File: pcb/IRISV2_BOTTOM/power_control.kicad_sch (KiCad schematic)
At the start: 49 parts, among them J10 Screw_Terminal_01x02, J11 Screw_Terminal_01x02, J12 Screw_Terminal_01x02, J13 Screw_Terminal_01x02, J14 Screw_Terminal_01x02, J15 Screw_Terminal_01x02, J16 Screw_Terminal_01x02, J9 Screw_Terminal_01x02, Q1 BC846, Q10 PJA3404A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

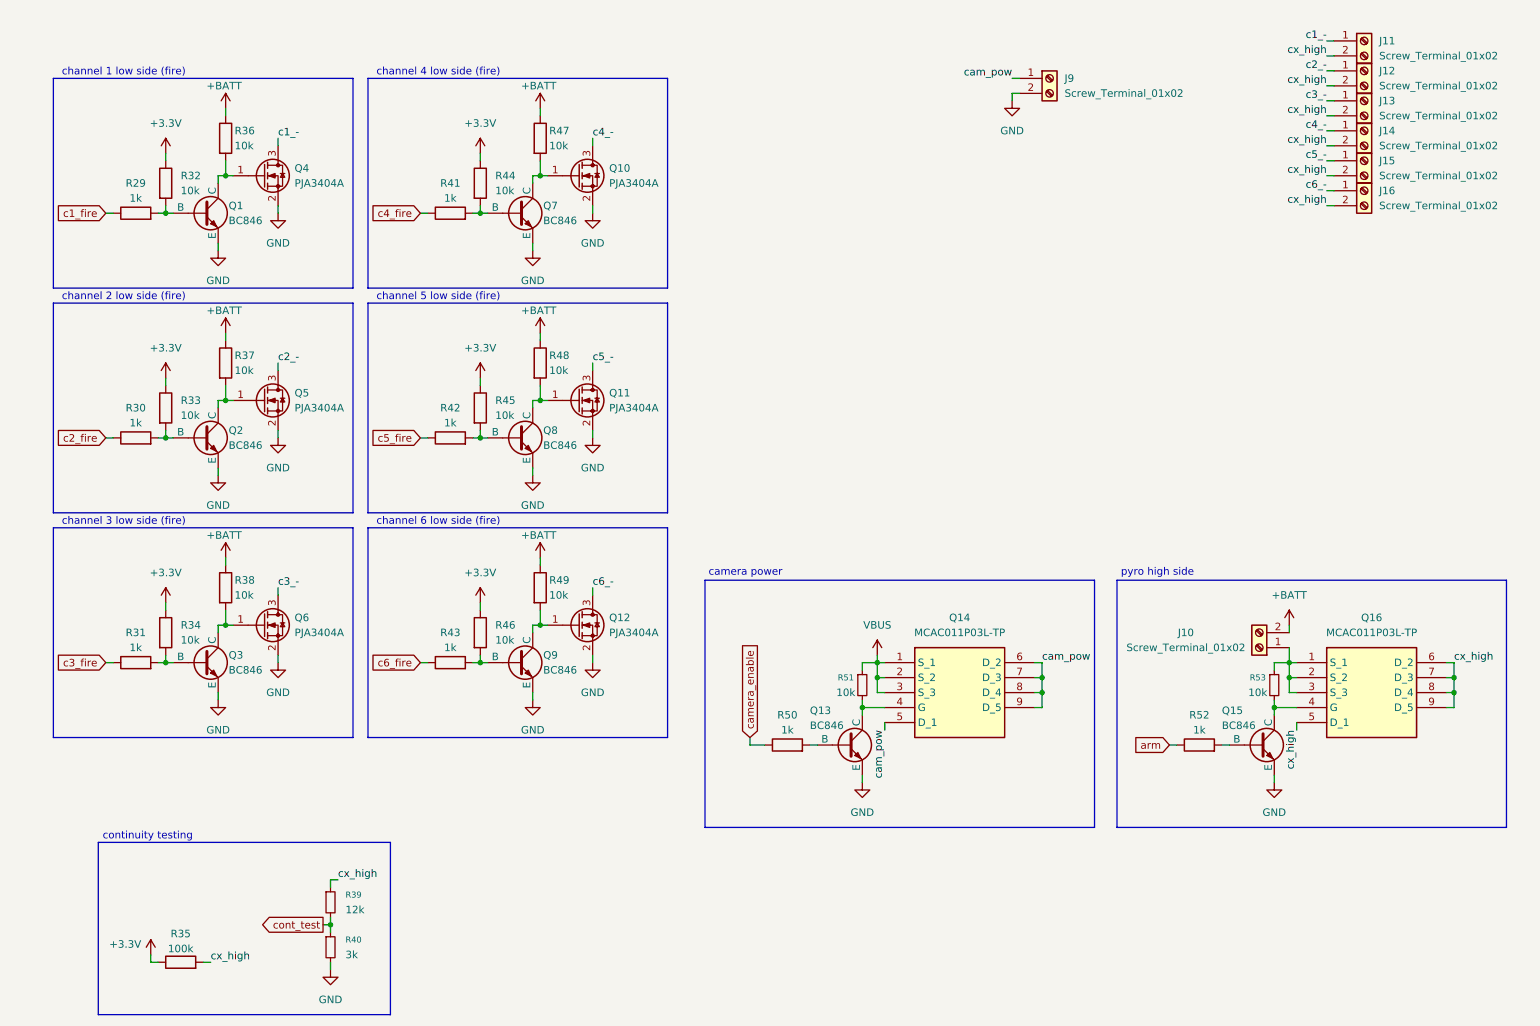
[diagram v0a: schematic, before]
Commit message: split into subprojects, fixed up stuff, started real pcb work
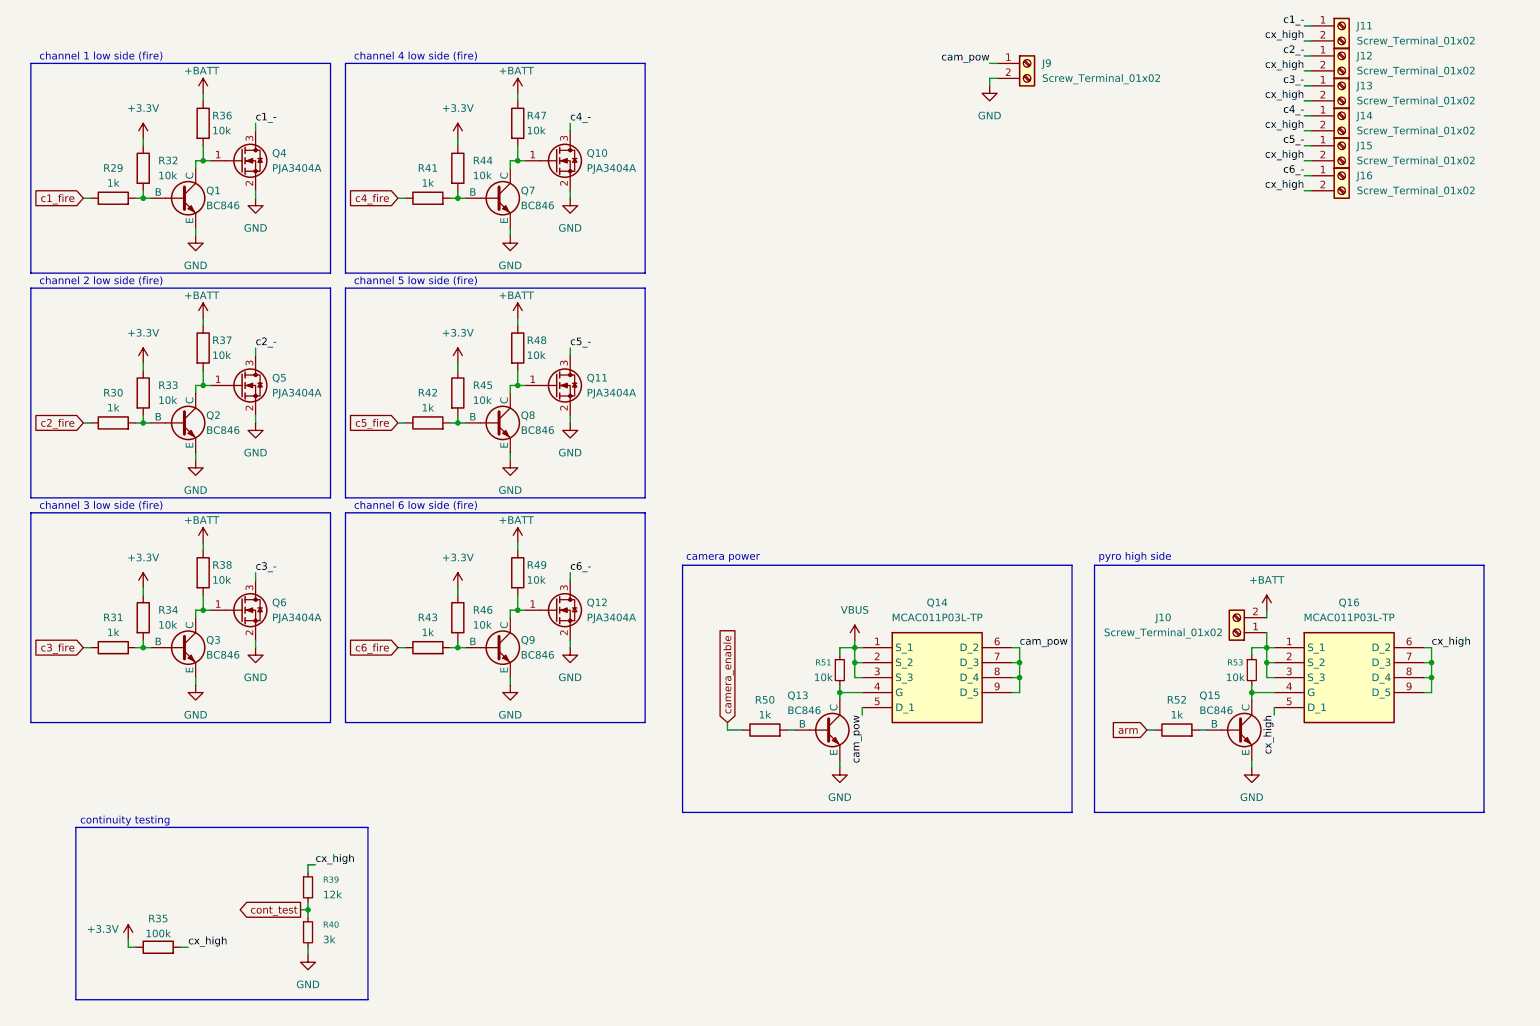
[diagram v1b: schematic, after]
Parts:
- Q1, Q10, Q11, Q12, Q13, Q15, Q2, Q3, Q4, Q5, Q6, Q7, Q8, Q9: footprint (none) -> Package_TO_SOT_SMD:SOT-23-3
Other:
- moved on the sheet: J10, J11, J12, J13, J14, J15, J16, J9, Q1, Q10, Q11, Q12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

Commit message: bottom pcb now mostly done, connectors selected - now need to finish integrating the connectors and other small tweaks to bottom routing
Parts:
- J10, J11, J12, J13, J14, J15, J16, J9: footprint (none) -> kf350-2p:kf350-2p
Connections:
- net GND: now also J9.1 (Pin_1); no longer J9.2 (Pin_2)
- net cam_pow: now also J9.2 (Pin_2); no longer J9.1 (Pin_1)
- net controlled_batt: now reaches J10.1 (Pin_1), Q16.1 (S_1), Q16.2 (S_2), Q16.3 (S_3), R53.1
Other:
- moved on the sheet: J9
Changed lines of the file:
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@@
 	(wire
 		(pts
-			(xy 185.42 33.02) (xy 186.69 33.02)
+			(xy 176.53 33.02) (xy 175.26 33.02)
 		)
 		(stroke
@@
 	(wire
 		(pts
+			(xy 176.53 35.56) (xy 175.26 35.56)
+		)
+		(stroke
+			(width 0)
+			(type default)
+		)
+	)
+	(wire
+		(pts
 			(xy 60.96 81.28) (xy 60.96 82.55)
 		)
@@
 	(wire
 		(pts
+			(xy 176.53 35.56) (xy 176.53 36.83)
+		)
+		(stroke
+			(width 0)
+			(type default)
+		)
+	)
+	(wire
+		(pts
 			(xy 85.09 93.98) (xy 86.36 93.98)
 		)
@@
 	(wire
 		(pts
-			(xy 185.42 35.56) (xy 185.42 36.83)
-		)
-		(stroke
-			(width 0)
-			(type default)
-		)
-	)
-	(wire
-		(pts
 			(xy 105.41 76.2) (xy 105.41 77.47)
 		)
@@
 	(wire
 		(pts
-			(xy 185.42 35.56) (xy 186.69 35.56)
-		)
-		(stroke
-			(width 0)
-			(type default)
-		)
-	)
-	(wire
-		(pts
 			(xy 238.76 29.21) (xy 240.03 29.21)
 		)
@@
 	)
 	(label "cam_pow"
-		(at 185.42 33.02 180)
+		(at 176.53 33.02 0)
 		(effects
 			(font
 				(size 1.27 1.27)
 			)
-			(justify right bottom)
+			(justify left bottom)
+		)
+	)
+	(label "controlled_batt"
+		(at 232.41 129.54 0)
+		(effects
+			(font
+				(size 1.27 1.27)
+			)
+			(justify left bottom)
 		)
 	)
@@
 			)
 		)
-		(property "Footprint" ""
+		(property "Footprint" "kf350-2p:kf350-2p"
 			(at 245.11 46.99 0)
 			(effects
@@
 	(symbol
 		(lib_id "Connector:Screw_Terminal_01x02")
-		(at 191.77 33.02 0)
+		(at 170.18 35.56 180)
 		(unit 1)
 		(exclude_from_sim no)
@@
 		(fields_autoplaced yes)
 		(property "Reference" "J9"
-			(at 194.31 33.0199 0)
+			(at 170.18 26.67 0)
 			(effects
 				(font
 					(size 1.27 1.27)
 				)
-				(justify left)
 			)
 		)
 		(property "Value" "Screw_Terminal_01x02"
-			(at 194.31 35.5599 0)
+			(at 170.18 29.21 0)
 			(effects
 				(font
 					(size 1.27 1.27)
 				)
-				(justify left)
 			)
 		)
-		(property "Footprint" ""
-			(at 191.77 33.02 0)
+		(property "Footprint" "kf350-2p:kf350-2p"
+			(at 170.18 35.56 0)
 			(effects
 				(font
@@
 		)
 		(property "Datasheet" "~"
-			(at 191.77 33.02 0)
+			(at 170.18 35.56 0)
 			(effects
 				(font
@@
 		)
 		(property "Description" "Generic screw terminal, single row, 01x02, script generated (kicad-library-utils/schlib/autogen/connector/)"
-			(at 191.77 33.02 0)
+			(at 170.18 35.56 0)
 			(effects
 				(font
@@
 			)
 		)
-		(property "Footprint" ""
+		(property "Footprint" "kf350-2p:kf350-2p"
 			(at 227.33 129.54 0)
 			(effects
@@
 	(symbol
 		(lib_id "power:GND")
-		(at 185.42 36.83 0)
+		(at 176.53 36.83 0)
 		(unit 1)
 		(exclude_from_sim no)
@@
 		(fields_autoplaced yes)
 		(property "Reference" "#PWR0168"
-			(at 185.42 43.18 0)
+			(at 176.53 43.18 0)
 			(effects
 				(font
@@
 		)
 		(property "Value" "GND"
-			(at 185.42 41.91 0)
+			(at 176.53 41.91 0)
 			(effects
 				(font
@@
 		)
 		(property "Footprint" ""
-			(at 185.42 36.83 0)
+			(at 176.53 36.83 0)
 			(effects
 				(font
@@
 		)
 		(property "Datasheet" ""
-			(at 185.42 36.83 0)
+			(at 176.53 36.83 0)
 			(effects
 				(font
@@
 		)
 		(property "Description" "Power symbol creates a global label with name \"GND\" , ground"
-			(at 185.42 36.83 0)
+			(at 176.53 36.83 0)
 			(effects
 				(font
@@
 			)
 		)
-		(property "Footprint" ""
+		(property "Footprint" "kf350-2p:kf350-2p"
 			(at 245.11 26.67 0)
 			(effects
@@
 			)
 		)
-		(property "Footprint" ""
+		(property "Footprint" "kf350-2p:kf350-2p"
 			(at 245.11 52.07 0)
 			(effects
@@
 			)
 		)
-		(property "Footprint" ""
+		(property "Footprint" "kf350-2p:kf350-2p"
 			(at 245.11 41.91 0)
 			(effects
@@
 			)
 		)
-		(property "Footprint" ""
+		(property "Footprint" "kf350-2p:kf350-2p"
 			(at 245.11 31.75 0)
 			(effects
@@
 			)
 		)
-		(property "Footprint" ""
+		(property "Footprint" "kf350-2p:kf350-2p"
 			(at 245.11 36.83 0)
 			(effects
